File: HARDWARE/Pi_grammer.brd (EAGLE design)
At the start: 58.4 x 78.7 mm, 27 parts, among them U1 AT42QT1010SOT23

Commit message: updated name
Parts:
- moved LOGO1 5.24 mm to (35.9, 74.9)
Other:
- board text added: "Pi_grammer"
- board text removed: "Pigrammer"
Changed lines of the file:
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@@
 <layer number="47" name="Measures" color="7" fill="1" visible="no" active="yes"/>
 <layer number="48" name="Document" color="7" fill="1" visible="no" active="yes"/>
-<layer number="49" name="Reference" color="7" fill="1" visible="yes" active="yes"/>
+<layer number="49" name="Reference" color="7" fill="1" visible="no" active="yes"/>
 <layer number="50" name="dxf" color="7" fill="1" visible="no" active="yes"/>
 <layer number="51" name="tDocu" color="6" fill="1" visible="yes" active="yes"/>
@@
 <wire x1="58.42" y1="2.54" x2="55.88" y2="0" width="0.254" layer="20" curve="-90"/>
 <wire x1="55.88" y1="0" x2="2.54" y2="0" width="0.254" layer="20"/>
-<text x="29.337" y="72.644" size="1.778" layer="21" font="vector" ratio="15">Pigrammer</text>
+<text x="28.067" y="72.644" size="1.778" layer="21" font="vector" ratio="15">Pi_grammer</text>
 <text x="6.7724375" y="75.946675" size="1.27" layer="21" font="vector" ratio="15">HARDWARE #</text>
 <text x="26.67" y="52.07" size="1.27" layer="21" font="vector" ratio="15" align="center-right">TEST SCRIPT RUNNING</text>
@@
 </element>
 <element name="D7" library="SparkFun-LED" package="LED-1206" value="GREEN" x="24.13" y="26.67" rot="R180"/>
-<element name="LOGO1" library="SparkFun-Aesthetics" package="SFE_LOGO_FLAME_.1" value="SFE_LOGO_FLAME.1_INCH" x="30.861" y="73.66"/>
+<element name="LOGO1" library="SparkFun-Aesthetics" package="SFE_LOGO_FLAME_.1" value="SFE_LOGO_FLAME.1_INCH" x="35.941" y="74.93"/>
 <element name="LOGO2" library="SparkFun-Aesthetics" package="OSHW-LOGO-S" value="OSHW-LOGOS" x="55.88" y="76.454"/>
 <element name="U1" library="SparkFun-DigitalIC" package="SOT23-6" value="AT42QT1010SOT23" x="35.56" y="17.78" rot="R270"/>

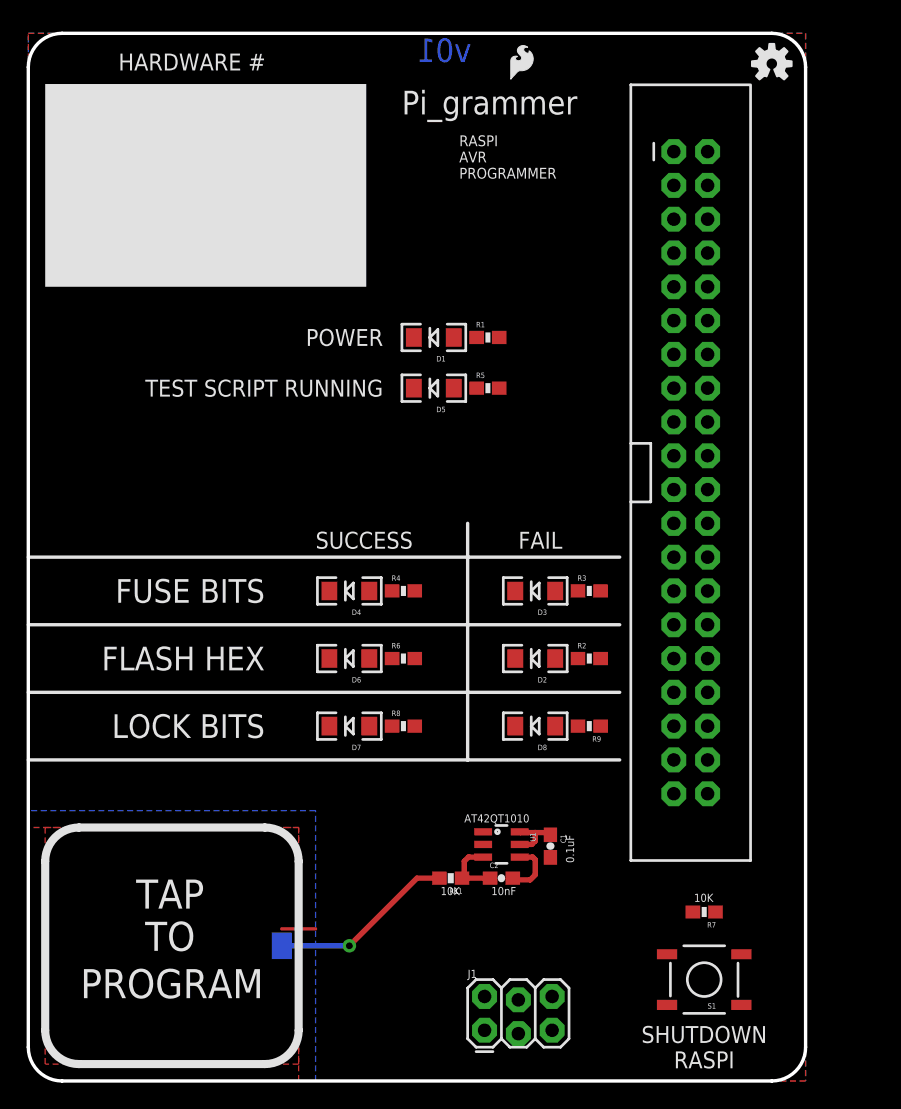
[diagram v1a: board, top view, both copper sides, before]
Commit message: Moved ISP 3x2 header to right side
I had to move header to avoid the bottom side of the pins hitting the
enclosure. The PCB is designed to sit flush on top of the raspi
enclosure.
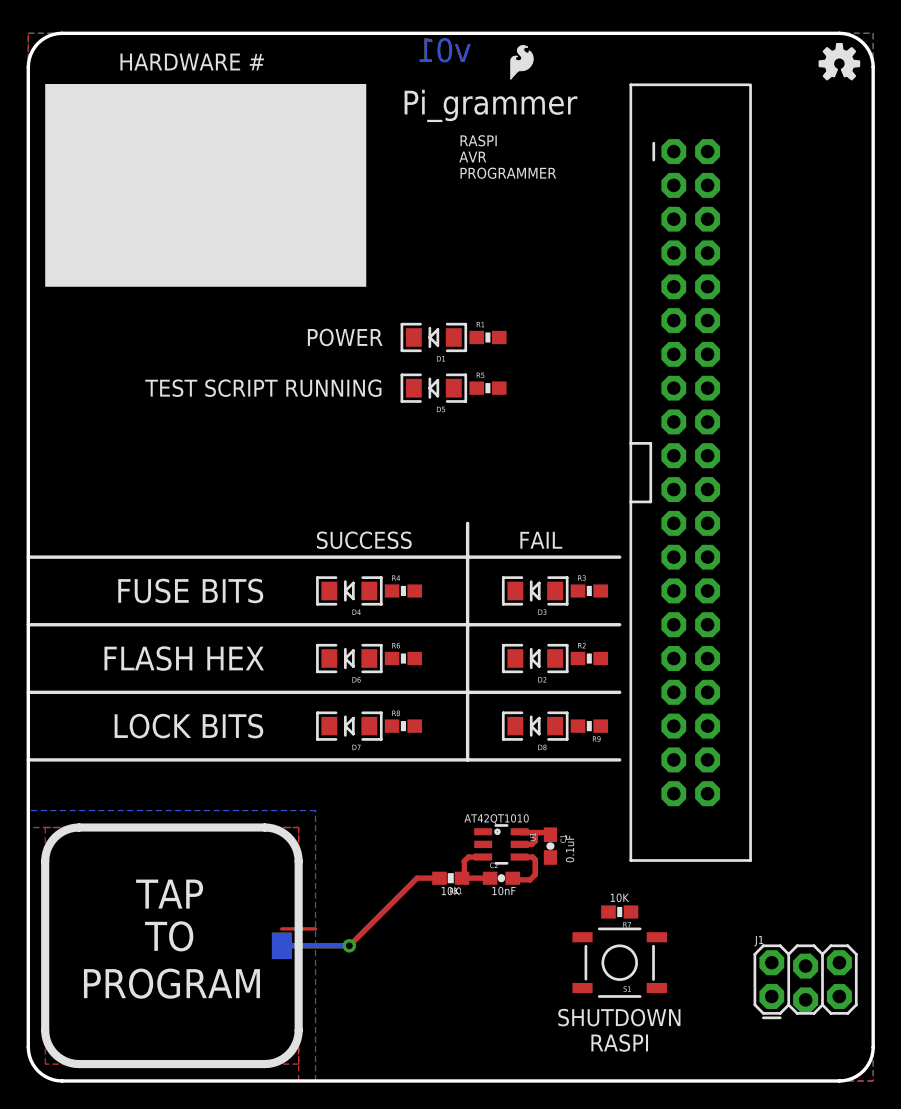
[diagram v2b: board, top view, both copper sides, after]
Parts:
- moved J1 21.7 mm to (55.9, 6.35)
- moved S1 6.48 mm to (44.5, 8.89)
- moved R7 6.35 mm to (44.5, 12.7)
- moved LOGO2 5.08 mm to (61.0, 76.5)
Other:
- board size 58.4 x 78.7 mm -> 63.5 x 78.7 mm
- board text added: "EDGE of raspi enclosure"
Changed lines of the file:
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@@
 <board>
 <plain>
-<wire x1="58.42" y1="76.2" x2="55.88" y2="78.74" width="0.254" layer="20" curve="90"/>
-<wire x1="55.88" y1="78.74" x2="2.54" y2="78.74" width="0.254" layer="20"/>
+<wire x1="63.5" y1="76.2" x2="60.96" y2="78.74" width="0.254" layer="20" curve="90"/>
+<wire x1="60.96" y1="78.74" x2="2.54" y2="78.74" width="0.254" layer="20"/>
 <wire x1="2.54" y1="78.74" x2="0" y2="76.2" width="0.254" layer="20" curve="90"/>
 <wire x1="0" y1="76.2" x2="0" y2="2.54" width="0.254" layer="20"/>
 <wire x1="0" y1="2.54" x2="2.54" y2="0" width="0.254" layer="20" curve="90"/>
-<wire x1="58.42" y1="76.2" x2="58.42" y2="2.54" width="0.254" layer="20"/>
-<wire x1="58.42" y1="2.54" x2="55.88" y2="0" width="0.254" layer="20" curve="-90"/>
-<wire x1="55.88" y1="0" x2="2.54" y2="0" width="0.254" layer="20"/>
+<wire x1="63.5" y1="76.2" x2="63.5" y2="2.54" width="0.254" layer="20"/>
+<wire x1="63.5" y1="2.54" x2="60.96" y2="0" width="0.254" layer="20" curve="-90"/>
+<wire x1="60.96" y1="0" x2="2.54" y2="0" width="0.254" layer="20"/>
 <text x="28.067" y="72.644" size="1.778" layer="21" font="vector" ratio="15">Pi_grammer</text>
 <text x="6.7724375" y="75.946675" size="1.27" layer="21" font="vector" ratio="15">HARDWARE #</text>
@@
 AVR
 PROGRAMMER</text>
-<text x="50.8" y="2.54" size="1.27" layer="21" font="vector" ratio="15" align="center">SHUTDOWN
+<text x="44.45" y="3.81" size="1.27" layer="21" font="vector" ratio="15" align="center">SHUTDOWN
 RASPI</text>
 <text x="17.78" y="31.75" size="1.778" layer="21" font="vector" ratio="15" align="center-right">FLASH HEX</text>
@@
 <text x="17.78" y="26.67" size="1.778" layer="21" font="vector" ratio="15" align="center-right">LOCK BITS</text>
 <text x="29.21" y="77.47" size="1.778" layer="16" font="vector" ratio="21" rot="MR0" align="center-right">v01</text>
-<text x="50.038" y="13.462" size="0.6096" layer="21" font="vector" ratio="15">10K</text>
+<text x="43.688" y="13.462" size="0.6096" layer="21" font="vector" ratio="15">10K</text>
 <text x="21.59" y="40.64" size="1.27" layer="21" font="vector" ratio="15" rot="R180" align="center-right">SUCCESS</text>
 <wire x1="20.32" y1="16.51" x2="17.78" y2="19.05" width="0.6096" layer="21" curve="90"/>
@@
 <text x="10.668" y="9.779" size="2.1844" layer="21" font="vector" ratio="15" align="bottom-center">TO</text>
 <text x="10.668" y="12.954" size="2.1844" layer="21" font="vector" ratio="15" align="bottom-center">TAP</text>
+<wire x1="54.61" y1="88.9" x2="54.61" y2="-13.97" width="0.254" layer="51" style="shortdash"/>
+<text x="53.34" y="81.28" size="1.778" layer="51" font="vector" ratio="15" rot="R90">EDGE of raspi enclosure</text>
 </plain>
 <attributes>
@@
 <attribute name="PROD_ID" value="RES-00818" x="28.194" y="31.75" size="1.778" layer="27" font="vector" ratio="15" display="off"/>
 </element>
-<element name="S1" library="SparkFun-Electromechanical" package="TACTILE-SWITCH-SMD" value="" x="50.8" y="7.62" rot="R180">
-<attribute name="PROD_ID" value="SWCH-08247" x="50.8" y="7.62" size="1.778" layer="27" font="vector" ratio="15" rot="R180" display="off"/>
-</element>
-<element name="R7" library="SparkFun-Resistors" package="0603-RES@1" value="10K" x="50.8" y="12.7" rot="R180">
-<attribute name="PROD_ID" value="RES-00818" x="50.8" y="12.7" size="1.778" layer="27" font="vector" ratio="15" rot="R180" display="off"/>
+<element name="S1" library="SparkFun-Electromechanical" package="TACTILE-SWITCH-SMD" value="" x="44.45" y="8.89" rot="R180">
+<attribute name="PROD_ID" value="SWCH-08247" x="44.45" y="8.89" size="1.778" layer="27" font="vector" ratio="15" rot="R180" display="off"/>
+</element>
+<element name="R7" library="SparkFun-Resistors" package="0603-RES@1" value="10K" x="44.45" y="12.7" rot="R180">
+<attribute name="PROD_ID" value="RES-00818" x="44.45" y="12.7" size="1.778" layer="27" font="vector" ratio="15" rot="R180" display="off"/>
 </element>
 <element name="R8" library="SparkFun-Resistors" package="0603-RES@1" value="1K" x="28.194" y="26.67">
@@
 <element name="D7" library="SparkFun-LED" package="LED-1206" value="GREEN" x="24.13" y="26.67" rot="R180"/>
 <element name="LOGO1" library="SparkFun-Aesthetics" package="SFE_LOGO_FLAME_.1" value="SFE_LOGO_FLAME.1_INCH" x="35.941" y="74.93"/>
-<element name="LOGO2" library="SparkFun-Aesthetics" package="OSHW-LOGO-S" value="OSHW-LOGOS" x="55.88" y="76.454"/>
+<element name="LOGO2" library="SparkFun-Aesthetics" package="OSHW-LOGO-S" value="OSHW-LOGOS" x="60.96" y="76.454"/>
 <element name="U1" library="SparkFun-DigitalIC" package="SOT23-6" value="AT42QT1010SOT23" x="35.56" y="17.78" rot="R270"/>
 <element name="C1" library="SparkFun-Capacitors" package="0603-CAP" value="0.1uF" x="39.243" y="17.653" rot="R270"/>
@@
 <element name="R11" library="SparkFun-Resistors" package="0603-RES" value="10k" x="31.75" y="15.24" rot="R180"/>
 <element name="JP9" library="SparkFun-Connectors" package="PAD-1.5X4.5" value="M01SMD-4.5X1.5" x="19.05" y="10.16" rot="MR0"/>
-<element name="J1" library="SparkFun-Connectors" package="2X3_LOCK" value="" x="34.29" y="3.81"/>
+<element name="J1" library="SparkFun-Connectors" package="2X3_LOCK" value="" x="55.88" y="6.35"/>
 <element name="D8" library="SparkFun-LED" package="LED-1206" value="RED" x="38.1" y="26.67" rot="R180"/>
 <element name="R9" library="SparkFun-Resistors" package="0603-RES@1" value="1K" x="42.164" y="26.67" rot="R180">
@@
 <polygon width="0.381" layer="16" isolate="0.381">
 <vertex x="0" y="78.74"/>
-<vertex x="58.42" y="78.74"/>
-<vertex x="58.42" y="0"/>
+<vertex x="63.5" y="78.74"/>
+<vertex x="63.5" y="0"/>
 <vertex x="21.59" y="0"/>
 <vertex x="21.59" y="20.32"/>
@@
 <polygon width="0.381" layer="1" isolate="0.381">
 <vertex x="0" y="78.74"/>
-<vertex x="58.42" y="78.74"/>
-<vertex x="58.42" y="0"/>
+<vertex x="63.5" y="78.74"/>
+<vertex x="63.5" y="0"/>
 <vertex x="20.32" y="0"/>
 <vertex x="20.32" y="19.05"/>
@@
 <wire x1="48.514" y1="49.53" x2="35.394" y2="55.88" width="0" layer="19" extent="1-1"/>
 <wire x1="39.077" y1="18.669" x2="48.514" y2="49.53" width="0" layer="19" extent="1-1"/>
-<wire x1="51.65" y1="12.7" x2="39.243" y2="18.503" width="0" layer="19" extent="1-1"/>
+<wire x1="45.3" y1="12.7" x2="39.243" y2="18.503" width="0" layer="19" extent="1-1"/>
 </signal>
 <signal name="TXO">
@@
 <contactref element="JP2" pad="18"/>
 <contactref element="J1" pad="3"/>
-<wire x1="36.83" y1="3.556" x2="51.054" y2="49.53" width="0" layer="19" extent="1-1"/>
+<wire x1="58.42" y1="6.096" x2="51.054" y2="49.53" width="0" layer="19" extent="1-1"/>
 </signal>
 <signal name="GP18">
 <contactref element="JP2" pad="12"/>
 <contactref element="J1" pad="1"/>
-<wire x1="34.29" y1="3.81" x2="51.054" y2="57.15" width="0" layer="19" extent="1-1"/>
+<wire x1="55.88" y1="6.35" x2="51.054" y2="57.15" width="0" layer="19" extent="1-1"/>
 </signal>
 <signal name="ID_SD">
@@
 <contactref element="JP2" pad="35"/>
 <contactref element="J1" pad="5"/>
-<wire x1="39.37" y1="3.81" x2="48.514" y2="26.67" width="0" layer="19" extent="1-1"/>
+<wire x1="60.96" y1="6.35" x2="48.514" y2="26.67" width="0" layer="19" extent="1-1"/>
 </signal>
 <signal name="GP20">
@@
 <contactref element="JP2" pad="16"/>
 <contactref element="J1" pad="4"/>
-<wire x1="36.83" y1="6.096" x2="51.054" y2="52.07" width="0" layer="19" extent="1-1"/>
+<wire x1="58.42" y1="8.636" x2="51.054" y2="52.07" width="0" layer="19" extent="1-1"/>
 </signal>
 <signal name="N$1">
@@
 <contactref element="S1" pad="1"/>
 <contactref element="JP2" pad="29"/>
-<wire x1="49.95" y1="12.7" x2="48.514" y2="34.29" width="0" layer="19" extent="1-1"/>
-<wire x1="53.594" y1="5.715" x2="49.95" y2="12.7" width="0" layer="19" extent="1-1"/>
+<wire x1="43.6" y1="12.7" x2="48.514" y2="34.29" width="0" layer="19" extent="1-1"/>
+<wire x1="47.244" y1="6.985" x2="43.6" y2="12.7" width="0" layer="19" extent="1-1"/>
 </signal>
 <signal name="N$5">
